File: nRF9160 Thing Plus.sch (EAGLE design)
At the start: 86 parts, among them J1 USB Female C, J10 QWIIC_RIGHT_ANGLE, J2 CON-HEADER-1X12-MALE-PIN, J3 CON-HEADER-1X16-MALE-PIN, J4 CON-1909763-1, J6 CON-S2B-PH-SM4-TB(LF)(SN), J7 CON-1909763-1, J9 CON-0002, P1 CON-SIM-SF72S006VBAR2500, Q1 MOSFET-P-SC89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

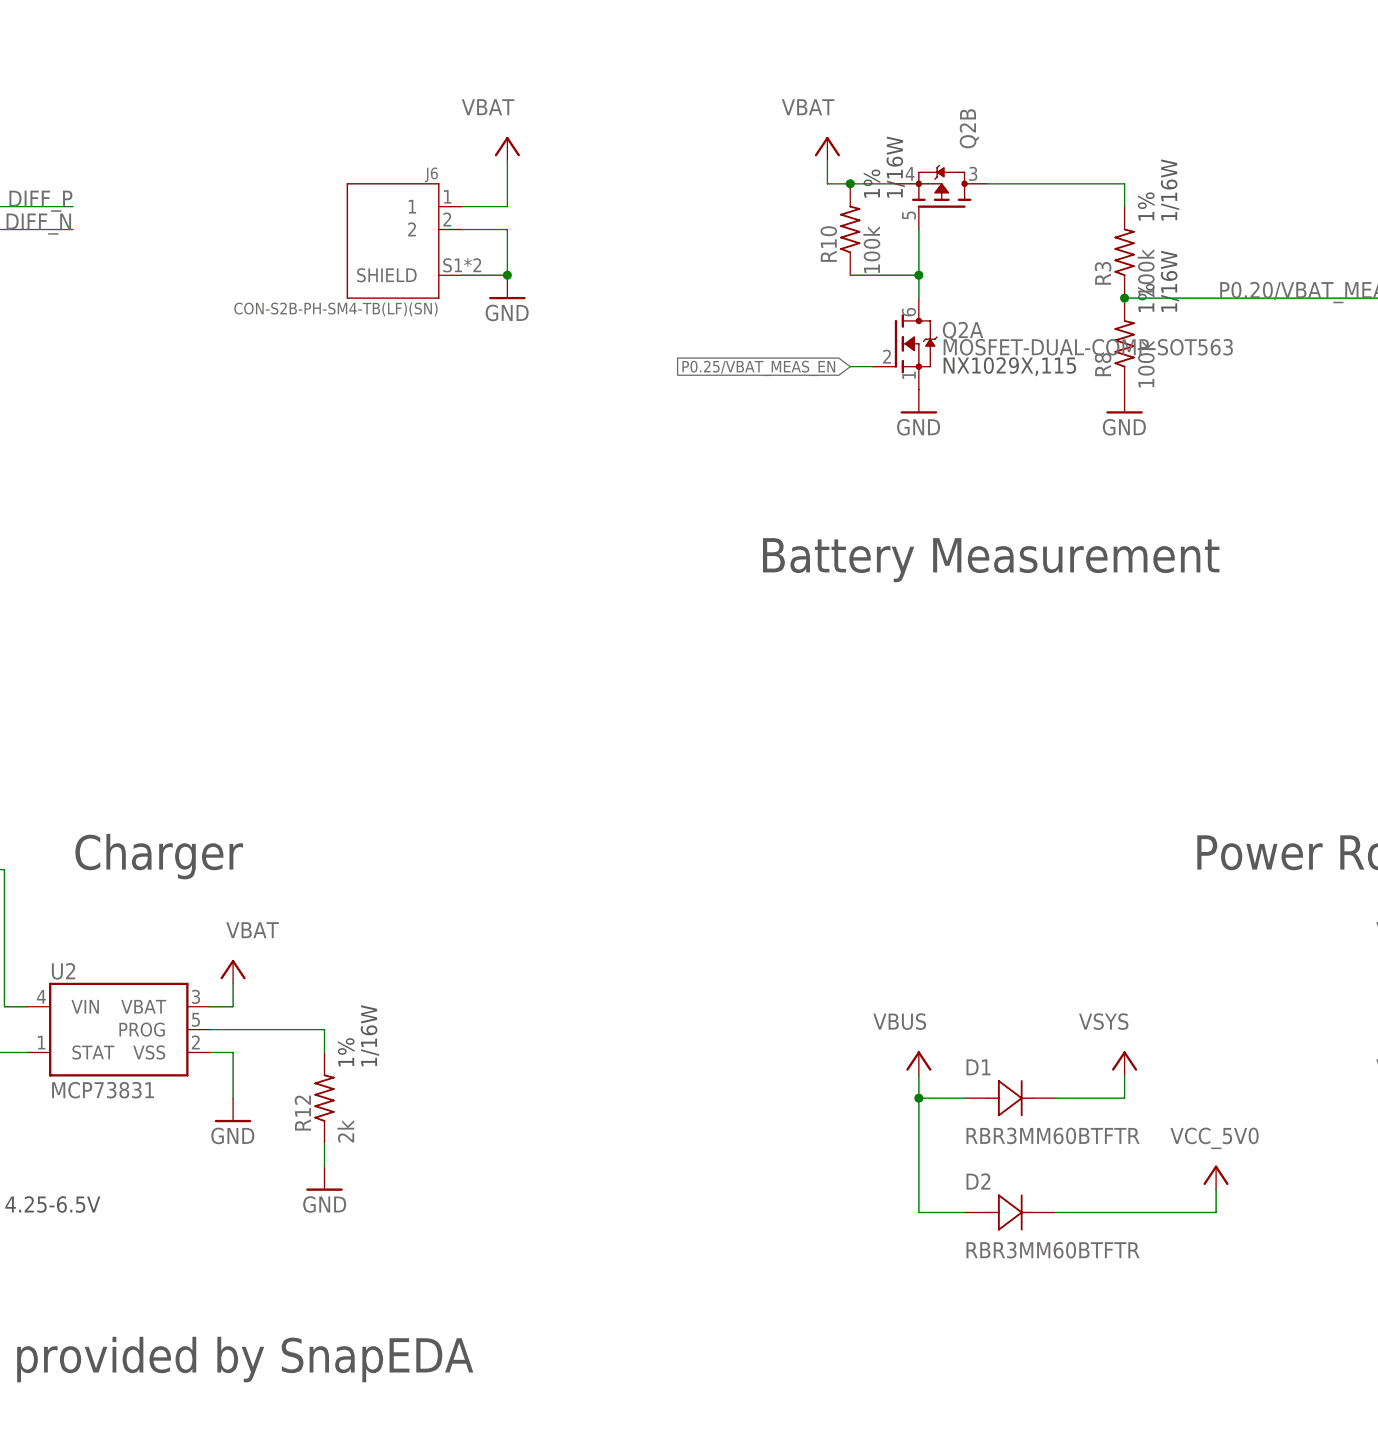
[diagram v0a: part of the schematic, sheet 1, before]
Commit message: Changed C9 to match other 4.7u caps. Update D5/D6 to BAT60A Updated J5 to match Sparkfun's JST connector
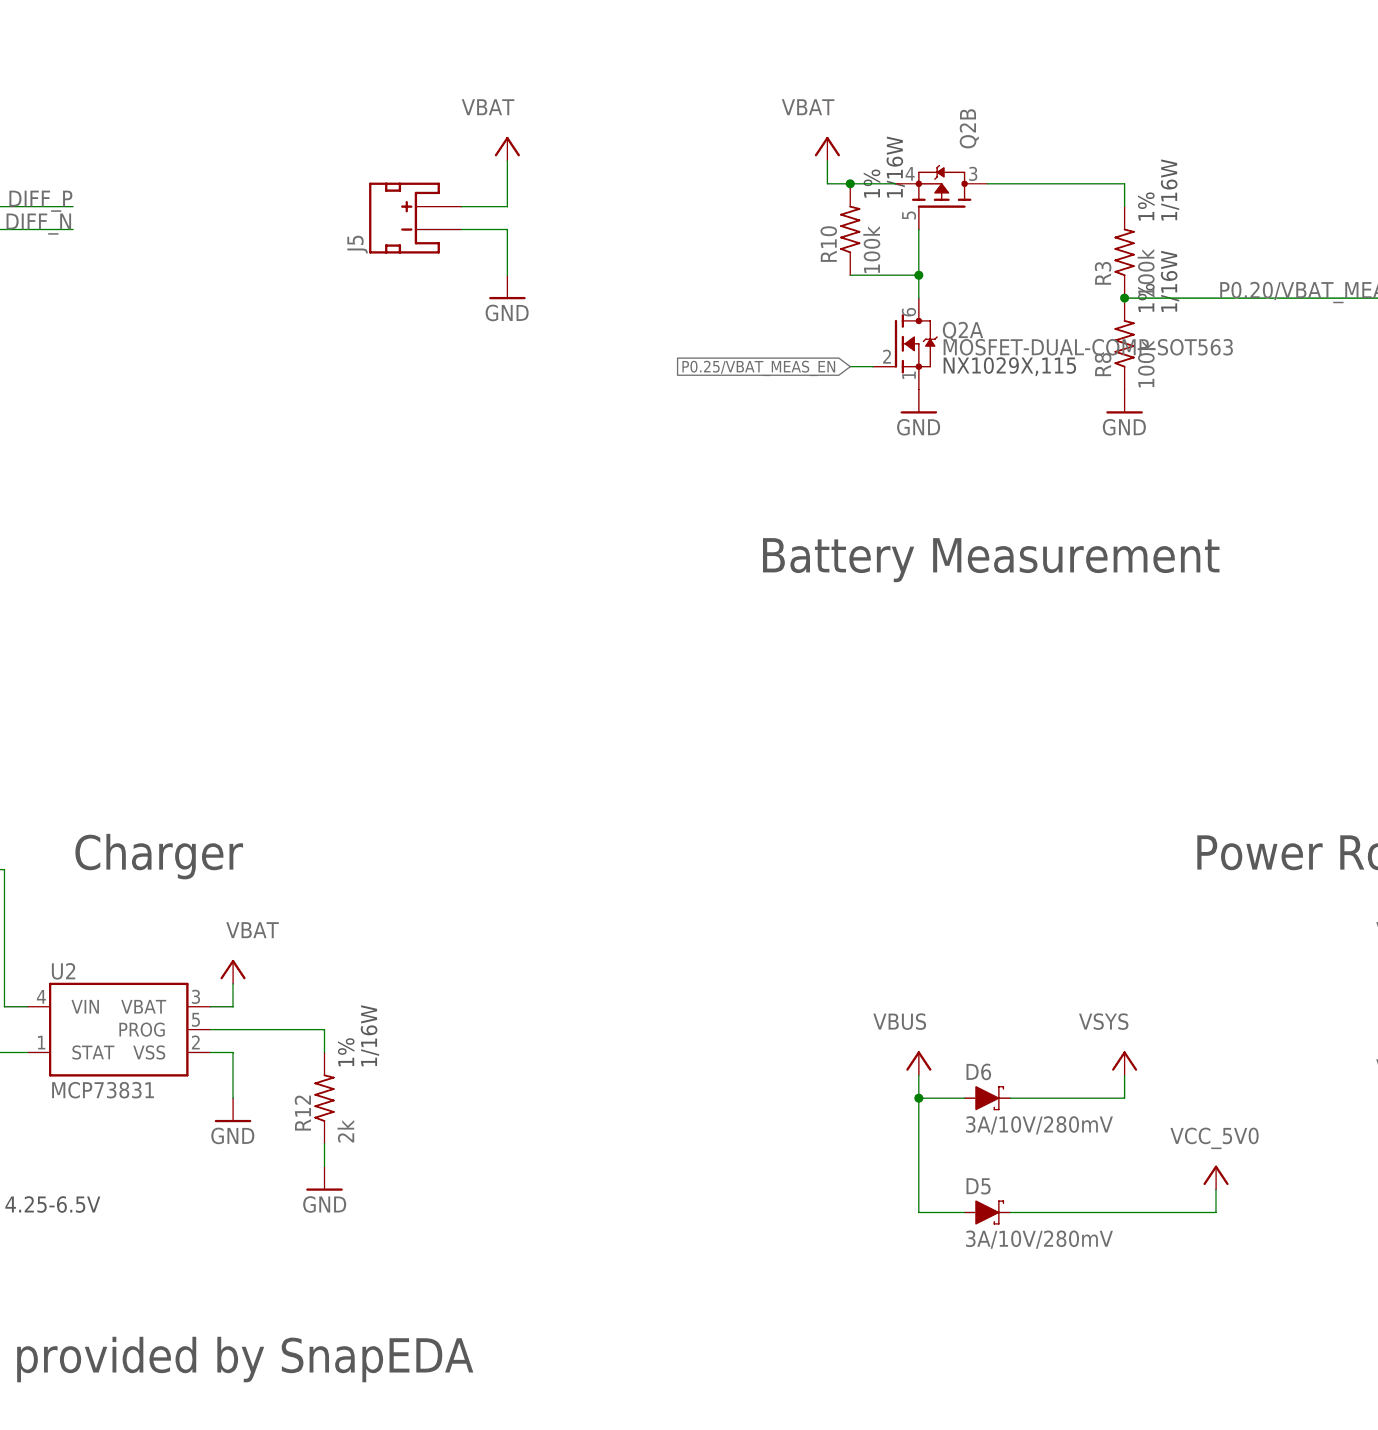
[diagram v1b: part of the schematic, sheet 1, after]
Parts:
- removed D1, D2: DIO-SCHOTTKY-3A-01, wolff-den:DIO-SCHOTTKY-3A-01
- removed J6: CON-S2B-PH-SM4-TB(LF)(SN), wolff-den:CON-S2B-PH-SM4-TB(LF)(SN)
- added D5, D6: 3A/10V/280mV, SparkFun-DiscreteSemi:DIODE-SCHOTTKY-BAT60A
- added J5: (no value), SparkFun-Connectors:JST_2MM_MALE
- C9: device wolff-den:CAP-4.7U-6.3V-0603 -> wolff-den:CAP-4.7U-6.3V-2-0603
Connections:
- net GND: now also J5.-; no longer J6.2, J6.SHIELD
- net VBAT: now also J5.+; no longer J6.1
- net VBUS: now also D5.A, D6.A; no longer D1.1, D2.1
- net VCC_5V0: now also D5.C; no longer D2.2
- net VSYS: now also D6.C; no longer D1.2
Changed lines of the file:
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@@
 <part name="Q3" library="wolff-den" library_urn="urn:adsk.eagle:library:6370453" deviceset="MOSFET-P" device="-SOT23" package3d_urn="urn:adsk.eagle:package:5807332/5" technology="-20V-4.7A" value="MOSFET-P-20V-4.7A-SOT23"/>
 <part name="P+1" library="wolff-den" library_urn="urn:adsk.eagle:library:6370453" deviceset="VBUS" device=""/>
-<part name="D1" library="wolff-den" library_urn="urn:adsk.eagle:library:6370453" deviceset="DIO-SCHOTTKY" device="" package3d_urn="urn:adsk.eagle:package:7658662/7" technology="-3A-01" value="DIO-SCHOTTKY-3A-01"/>
 <part name="P+2" library="wolff-den" library_urn="urn:adsk.eagle:library:6370453" deviceset="VBUS" device=""/>
 <part name="P+4" library="wolff-den" library_urn="urn:adsk.eagle:library:6370453" deviceset="VSYS" device=""/>
@@
 <part name="+3V2" library="supply1" library_urn="urn:adsk.eagle:library:371" deviceset="+3V3" device=""/>
 <part name="P+7" library="wolff-den" library_urn="urn:adsk.eagle:library:6370453" deviceset="VCC_5V0" device=""/>
-<part name="D2" library="wolff-den" library_urn="urn:adsk.eagle:library:6370453" deviceset="DIO-SCHOTTKY" device="" package3d_urn="urn:adsk.eagle:package:7658662/7" technology="-3A-01" value="DIO-SCHOTTKY-3A-01"/>
 <part name="P+3" library="wolff-den" library_urn="urn:adsk.eagle:library:6370453" deviceset="VCC_5V0" device=""/>
 <part name="R7" library="wolff-den" library_urn="urn:adsk.eagle:library:6370453" deviceset="RES" device="-0402" package3d_urn="urn:adsk.eagle:package:19061974/2" technology="-100K-1%" value="100k"/>
@@
 <part name="C3" library="wolff-den" library_urn="urn:adsk.eagle:library:6370453" deviceset="CAP" device="-0603" package3d_urn="urn:adsk.eagle:package:5807321/6" technology="-4.7U-6.3V-2" value="4.7u"/>
 <part name="C8" library="wolff-den" library_urn="urn:adsk.eagle:library:6370453" deviceset="CAP" device="-0603" package3d_urn="urn:adsk.eagle:package:5807321/6" technology="-4.7U-6.3V-2" value="4.7u"/>
-<part name="C9" library="wolff-den" library_urn="urn:adsk.eagle:library:6370453" deviceset="CAP" device="-0603" package3d_urn="urn:adsk.eagle:package:5807321/6" technology="-4.7U-6.3V" value="4.7u"/>
+<part name="C9" library="wolff-den" library_urn="urn:adsk.eagle:library:6370453" deviceset="CAP" device="-0603" package3d_urn="urn:adsk.eagle:package:5807321/6" technology="-4.7U-6.3V-2" value="4.7u"/>
 <part name="GND9" library="supply1" library_urn="urn:adsk.eagle:library:371" deviceset="GND" device=""/>
 <part name="GND11" library="supply1" library_urn="urn:adsk.eagle:library:371" deviceset="GND" device=""/>
@@
 <part name="+3V11" library="supply1" library_urn="urn:adsk.eagle:library:371" deviceset="+3V3" device=""/>
 <part name="GND31" library="supply1" library_urn="urn:adsk.eagle:library:371" deviceset="GND" device=""/>
-<part name="J6" library="wolff-den" library_urn="urn:adsk.eagle:library:6370453" deviceset="CON-S2B-PH-SM4-TB(LF)(SN)" device="" package3d_urn="urn:adsk.eagle:package:19415242/2" override_package3d_urn="urn:adsk.eagle:package:19415993/2" override_package_urn="urn:adsk.eagle:footprint:19415233/1" override_locally_modified="yes"/>
 <part name="GND23" library="supply1" library_urn="urn:adsk.eagle:library:371" deviceset="GND" device=""/>
 <part name="P+17" library="wolff-den" library_urn="urn:adsk.eagle:library:6370453" deviceset="VSYS" device=""/>
@@
 <part name="GND50" library="supply1" library_urn="urn:adsk.eagle:library:371" deviceset="GND" device=""/>
 <part name="P1" library="wolff-den" library_urn="urn:adsk.eagle:library:6370453" deviceset="CON-SIM-SF72S006VBAR2500" device="" override_package3d_urn="urn:adsk.eagle:package:23317369/2" override_package_urn="urn:adsk.eagle:footprint:23317371/1"/>
+<part name="J5" library="SparkFun-Connectors" library_urn="urn:adsk.eagle:library:513" deviceset="JST_2MM_MALE" device="" package3d_urn="urn:adsk.eagle:package:38042/1"/>
+<part name="D5" library="SparkFun-DiscreteSemi" deviceset="DIODE-SCHOTTKY" device="-BAT60A" value="3A/10V/280mV"/>
+<part name="D6" library="SparkFun-DiscreteSemi" deviceset="DIODE-SCHOTTKY" device="-BAT60A" value="3A/10V/280mV"/>
 </parts>
 <sheets>
@@
 <attribute name="VALUE" x="228.6" y="40.64" size="1.778" layer="96"/>
 </instance>
-<instance part="D1" gate="A" x="182.88" y="38.1" smashed="yes">
-<attribute name="NAME" x="182.88" y="40.64" size="1.778" layer="95" ratio="10" rot="SR0"/>
-<attribute name="MPN" x="182.88" y="33.02" size="1.778" layer="96" ratio="10" rot="SR0"/>
-</instance>
 <instance part="P+2" gate="A" x="177.8" y="43.18" smashed="yes">
 <attribute name="VALUE" x="172.72" y="45.72" size="1.778" layer="96"/>
@@
 <instance part="P+7" gate="A" x="276.86" y="220.98" smashed="yes">
 <attribute name="VALUE" x="271.78" y="223.52" size="1.778" layer="96"/>
-</instance>
-<instance part="D2" gate="A" x="182.88" y="25.4" smashed="yes">
-<attribute name="NAME" x="182.88" y="27.94" size="1.778" layer="95" ratio="10" rot="SR0"/>
-<attribute name="MPN" x="182.88" y="20.32" size="1.778" layer="96" ratio="10" rot="SR0"/>
 </instance>
 <instance part="P+3" gate="A" x="210.82" y="30.48" smashed="yes">
@@
 <attribute name="NAME" x="184.15" y="143.51" size="1.778" layer="95" rot="R90"/>
 </instance>
-<instance part="J6" gate="G$1" x="119.38" y="134.62" smashed="yes" rot="MR0">
-<attribute name="NAME" x="124.4629" y="140.21571875" size="1.272509375" layer="95" rot="MR0"/>
-<attribute name="VALUE" x="124.46811875" y="125.19731875" size="1.275409375" layer="96" rot="MR0"/>
-</instance>
 <instance part="GND23" gate="1" x="132.08" y="127" smashed="yes">
 <attribute name="VALUE" x="129.54" y="124.46" size="1.778" layer="96"/>
@@
 <attribute name="NAME" x="330.2" y="122.92" size="1.778" layer="95" ratio="10" rot="SR0"/>
 <attribute name="VALUE" x="330.2" y="73.66" size="1.778" layer="96" ratio="10" rot="SR0"/>
+</instance>
+<instance part="J5" gate="G$1" x="121.92" y="134.62" smashed="yes" rot="R90">
+<attribute name="NAME" x="116.078" y="132.08" size="1.778" layer="95" rot="R90"/>
+</instance>
+<instance part="D5" gate="G$1" x="185.42" y="25.4" smashed="yes">
+<attribute name="NAME" x="182.88" y="27.432" size="1.778" layer="95" font="vector"/>
+<attribute name="VALUE" x="182.88" y="23.368" size="1.778" layer="96" font="vector" align="top-left"/>
+</instance>
+<instance part="D6" gate="G$1" x="185.42" y="38.1" smashed="yes">
+<attribute name="NAME" x="182.88" y="40.132" size="1.778" layer="95" font="vector"/>
+<attribute name="VALUE" x="182.88" y="36.068" size="1.778" layer="96" font="vector" align="top-left"/>
 </instance>
 </instances>
@@
 </segment>
 <segment>
-<pinref part="J6" gate="G$1" pin="SHIELD"/>
-<pinref part="J6" gate="G$1" pin="2"/>
-<wire x1="132.08" y1="129.54" x2="127" y2="129.54" width="0.1524" layer="91"/>
 <wire x1="127" y1="134.62" x2="132.08" y2="134.62" width="0.1524" layer="91"/>
 <wire x1="132.08" y1="134.62" x2="132.08" y2="129.54" width="0.1524" layer="91"/>
 <pinref part="GND23" gate="1" pin="GND"/>
-<junction x="132.08" y="129.54"/>
+<pinref part="J5" gate="G$1" pin="-"/>
 </segment>
 <segment>
@@
 </segment>
 <segment>
-<pinref part="D1" gate="A" pin="1"/>
 <wire x1="182.88" y1="38.1" x2="177.8" y2="38.1" width="0.1524" layer="91"/>
 <pinref part="P+2" gate="A" pin="VBUS"/>
@@
 <wire x1="177.8" y1="38.1" x2="177.8" y2="25.4" width="0.1524" layer="91"/>
 <junction x="177.8" y="38.1"/>
-<pinref part="D2" gate="A" pin="1"/>
 <wire x1="177.8" y1="25.4" x2="182.88" y2="25.4" width="0.1524" layer="91"/>
+<pinref part="D5" gate="G$1" pin="A"/>
+<pinref part="D6" gate="G$1" pin="A"/>
 </segment>
 <segment>
@@
 <pinref part="P+14" gate="G$1" pin="VBAT"/>
 <wire x1="132.08" y1="137.16" x2="132.08" y2="142.24" width="0.1524" layer="91"/>
-<pinref part="J6" gate="G$1" pin="1"/>
 <wire x1="132.08" y1="137.16" x2="127" y2="137.16" width="0.1524" layer="91"/>
+<pinref part="J5" gate="G$1" pin="+"/>
 </segment>
 <segment>
@@
 </segment>
 <segment>
-<pinref part="D1" gate="A" pin="2"/>
-<wire x1="193.04" y1="38.1" x2="200.66" y2="38.1" width="0.1524" layer="91"/>
+<wire x1="187.96" y1="38.1" x2="200.66" y2="38.1" width="0.1524" layer="91"/>
 <pinref part="P+4" gate="G$2" pin="VSYS"/>
 <wire x1="200.66" y1="38.1" x2="200.66" y2="40.64" width="0.1524" layer="91"/>
+<pinref part="D6" gate="G$1" pin="C"/>
 </segment>
 <segment>
@@
 </segment>
 <segment>
-<pinref part="D2" gate="A" pin="2"/>
-<wire x1="193.04" y1="25.4" x2="210.82" y2="25.4" width="0.1524" layer="91"/>
+<wire x1="187.96" y1="25.4" x2="210.82" y2="25.4" width="0.1524" layer="91"/>
 <pinref part="P+3" gate="A" pin="VCC_5V0"/>
 <wire x1="210.82" y1="25.4" x2="210.82" y2="27.94" width="0.1524" layer="91"/>
+<pinref part="D5" gate="G$1" pin="C"/>
 </segment>
 </net>

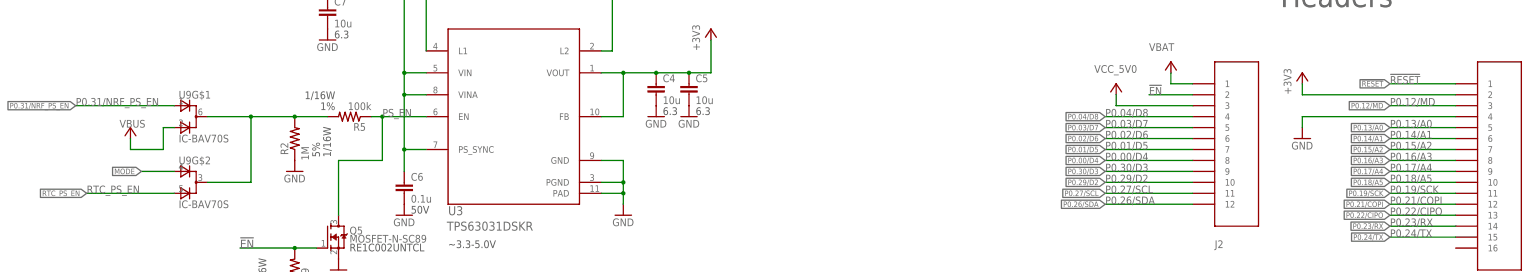
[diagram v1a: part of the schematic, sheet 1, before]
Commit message: Modifying mode pin to be connected directly to the MD button. (useful for external wakeup)
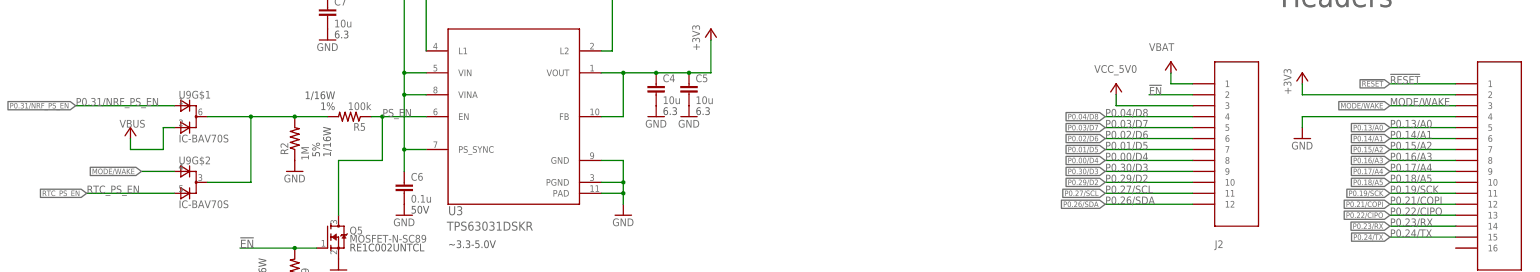
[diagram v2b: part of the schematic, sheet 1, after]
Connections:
- removed net MODE: Q4.G, R13.2, SW2.2, U9G$2.A1
- new net MODE/WAKE: J3.3, Q4.G, R13.2, SW2.2, U9G$2.A1
- net P0.12/MD: no longer J3.3
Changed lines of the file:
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@@
-</segment>
-</net>
-<net name="P0.12/MD" class="0">
-<segment>
-<wire x1="355.6" y1="215.9" x2="340.36" y2="215.9" width="0.1524" layer="91"/>
-<label x="340.36" y="215.9" size="1.778" layer="95"/>
-<pinref part="J3" gate="G$1" pin="3"/>
-<label x="340.36" y="215.9" size="1.27" layer="95" rot="R180" xref="yes"/>
 </segment>
 </net>
@@
 </segment>
 </net>
-<net name="MODE" class="0">
+<net name="MODE/WAKE" class="0">
 <segment>
 <wire x1="58.42" y1="200.66" x2="50.8" y2="200.66" width="0.1524" layer="91"/>
 <label x="50.8" y="200.66" size="1.27" layer="95" rot="MR0" xref="yes"/>
 <pinref part="U9" gate="G$2" pin="A1"/>
+</segment>
+<segment>
+<wire x1="355.6" y1="215.9" x2="340.36" y2="215.9" width="0.1524" layer="91"/>
+<label x="340.36" y="215.9" size="1.778" layer="95"/>
+<pinref part="J3" gate="G$1" pin="3"/>
+<label x="340.36" y="215.9" size="1.27" layer="95" rot="R180" xref="yes"/>
 </segment>
 </net>
@@
 </segment>
 </net>
-<net name="MODE" class="0">
+<net name="MODE/WAKE" class="0">
 <segment>
 <pinref part="Q4" gate="A" pin="G"/>
 <pinref part="SW2" gate="G$1" pin="2"/>
 <wire x1="76.2" y1="45.72" x2="68.58" y2="45.72" width="0.1524" layer="91"/>
-<label x="66.04" y="45.72" size="1.778" layer="95"/>
 <wire x1="68.58" y1="45.72" x2="58.42" y2="45.72" width="0.1524" layer="91"/>
 <wire x1="68.58" y1="45.72" x2="68.58" y2="33.02" width="0.1524" layer="91"/>

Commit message: Adding LIS2DH12TR and supporting components. Adding jumpers for D2 (Accel int) and also PS_EN
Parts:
- added C20: 0.1u, wolff-den:CAP-0.1U-50V-0402
- added JMP1: JUMPER-NC, wolff-den:JUMPER-NC
- added JMP2: JUMPER-3/1, wolff-den:JUMPER-3/1
- added R23: 100k, wolff-den:RES-100K-1%-0402
- added U12: IC-LIS2DH12TR, wolff-den:IC-LIS2DH12TR
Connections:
- new net N$11: R23.1, U12.CS
- new net N$12: JMP1.1, U12.INT1
- new net NRF_PS_EN_JMP: JMP2.2, U9G$1.A1
- net +3V3: now also C20.1, R23.2, U12.VDD, U12.VDD_IO
- net GND: now also C20.2, U12.GND, U12.RES, U12.SDO/SAO
- net P0.26/SDA: now also U12.SDA/SDI/SDO
- net P0.27/SCL: now also U12.SCL/SPC
- net P0.29/D2: now also JMP1.2
- net P0.31/NRF_PS_EN: now also J3.16, JMP2.3; no longer U9G$1.A1
- net VSYS: now also JMP2.1
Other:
- note added: "1.71-3.6V"
- note added: "Accelerometer"
